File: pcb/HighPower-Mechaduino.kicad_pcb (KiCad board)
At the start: 2 copper layers, 60 x 60 mm, 132 parts, among them J1 SUPPLY, J2 STEPPER, P1 SWD, P2 USB, P3 PoStep25-32, P4 CONN_01X04, Q1 SSM3J328R, Q10 IPD079N06L3G, Q11 BSS138, Q2 BSS138, Q3 IPD079N06L3G, Q4 IPD079N06L3G, Q5 IPD079N06L3G, Q6 IPD079N06L3G, Q7 IPD079N06L3G, Q8 IPD079N06L3G, Q9 IPD079N06L3G, SW1 B3U-1000P, U1 AS5047D, U2 AP2112K-3.3TRG1, U3 AT24CS64-SSHM, U4 SAMD21G18A-A, U5 A4955GLPTR-T, U6 A4955GLPTR-T, U7 USBLC6-2SC6, U8 MCP16331T, U9 LM75BD, Y1 G83270022

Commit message: Update schematic
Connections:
- P1 pad 6: (no net) -> Net-(P1-Pad6)
- P1 pad 8: (no net) -> Net-(P1-Pad8)
- P2 pad 4: (no net) -> /Protected_USB_Supply/ID
- U1 pad 10: (no net) -> Net-(U1-Pad10)
- U1 pad 14: (no net) -> Net-(U1-Pad14)
- U1 pad 6: (no net) -> Net-(U1-Pad6)
- U1 pad 7: (no net) -> Net-(U1-Pad7)
- U1 pad 8: (no net) -> Net-(U1-Pad8)
- U1 pad 9: (no net) -> Net-(U1-Pad9)
- U4 pad 14: (no net) -> /Arduino_Zero_Base/Arduino_D3
- U4 pad 15: (no net) -> /Arduino_Zero_Base/Arduino_D1
- U4 pad 16: (no net) -> /Arduino_Zero_Base/Arduino_D0
- U4 pad 22: (no net) -> Net-(U4-Pad22)
- U4 pad 39: (no net) -> /Arduino_Zero_Base/Arduino_TX_LED
- U4 pad 41: (no net) -> /Arduino_Zero_Base/Arduino_USB_HOST_ENABLED
- U4 pad 48: (no net) -> /Arduino_Zero_Base/Arduino_RX_LED
- U5 pad 9: (no net) -> /PWM_Bridge_A4955-A/SLEEPn
- U6 pad 9: (no net) -> /PWM_Bridge_A4955-B/SLEEPn
- U9 pad 3: (no net) -> Net-(U9-Pad3)
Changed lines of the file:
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@@
   (general
     (links 293)
-    (no_connects 1)
+    (no_connects 0)
     (area 119.924999 69.924999 180.075001 130.075001)
     (thickness 1.6)
@@
     (zones 0)
     (modules 132)
-    (nets 80)
+    (nets 99)
   )
   (page A4)
@@
   (net 78 /MCP16331_5V/Vfb)
   (net 79 "Net-(C33-Pad1)")
+  (net 80 "Net-(P1-Pad6)")
+  (net 81 "Net-(P1-Pad8)")
+  (net 82 "Net-(U1-Pad6)")
+  (net 83 "Net-(U1-Pad7)")
+  (net 84 "Net-(U1-Pad8)")
+  (net 85 "Net-(U1-Pad9)")
+  (net 86 "Net-(U1-Pad10)")
+  (net 87 "Net-(U1-Pad14)")
+  (net 88 /PWM_Bridge_A4955-A/SLEEPn)
+  (net 89 /PWM_Bridge_A4955-B/SLEEPn)
+  (net 90 "Net-(U9-Pad3)")
+  (net 91 /Arduino_Zero_Base/Arduino_D3)
+  (net 92 /Arduino_Zero_Base/Arduino_D1)
+  (net 93 /Arduino_Zero_Base/Arduino_D0)
+  (net 94 "Net-(U4-Pad22)")
+  (net 95 /Arduino_Zero_Base/Arduino_TX_LED)
+  (net 96 /Arduino_Zero_Base/Arduino_USB_HOST_ENABLED)
+  (net 97 /Arduino_Zero_Base/Arduino_RX_LED)
+  (net 98 /Protected_USB_Supply/ID)
   (net_class Default "Dies ist die voreingestellte Netzklasse."
     (clearance 0.15)
@@
     (add_net /A_IN)
     (add_net /Arduino_Zero_Base/Arduino_AREF)
+    (add_net /Arduino_Zero_Base/Arduino_D0)
+    (add_net /Arduino_Zero_Base/Arduino_D1)
+    (add_net /Arduino_Zero_Base/Arduino_D3)
     (add_net /Arduino_Zero_Base/Arduino_RXD)
+    (add_net /Arduino_Zero_Base/Arduino_RX_LED)
     (add_net /Arduino_Zero_Base/Arduino_TXD)
+    (add_net /Arduino_Zero_Base/Arduino_TX_LED)
+    (add_net /Arduino_Zero_Base/Arduino_USB_HOST_ENABLED)
     (add_net /IN1)
     (add_net /IN2)
@@
     (add_net /OCLn1)
     (add_net /OCLn2)
+    (add_net /PWM_Bridge_A4955-A/SLEEPn)
     (add_net /PWM_Bridge_A4955-A/VREF)
+    (add_net /PWM_Bridge_A4955-B/SLEEPn)
     (add_net /PWM_Bridge_A4955-B/VREF)
+    (add_net /Protected_USB_Supply/ID)
     (add_net /Protected_USB_Supply/VBUS)
     (add_net /RESET)
@@
     (add_net "Net-(F2-Pad1)")
     (add_net "Net-(L2-Pad1)")
+    (add_net "Net-(P1-Pad6)")
+    (add_net "Net-(P1-Pad8)")
     (add_net "Net-(P3-Pad7)")
     (add_net "Net-(Q1-Pad1)")
@@
     (add_net "Net-(R18-Pad1)")
     (add_net "Net-(R4-Pad1)")
+    (add_net "Net-(U1-Pad10)")
+    (add_net "Net-(U1-Pad14)")
+    (add_net "Net-(U1-Pad6)")
+    (add_net "Net-(U1-Pad7)")
+    (add_net "Net-(U1-Pad8)")
+    (add_net "Net-(U1-Pad9)")
+    (add_net "Net-(U4-Pad22)")
+    (add_net "Net-(U9-Pad3)")
     (add_net VDD)
   )
@@
     (pad 4 smd rect (at -2.7 1.905 180) (size 1.55 0.6) (layers F.Cu F.Paste F.Mask)
       (net 1 GND))
-    (pad 3 smd rect (at -2.7 0.635 180) (size 1.55 0.6) (layers F.Cu F.Paste F.Mask))
+    (pad 3 smd rect (at -2.7 0.635 180) (size 1.55 0.6) (layers F.Cu F.Paste F.Mask)
+      (net 90 "Net-(U9-Pad3)"))
     (pad 2 smd rect (at -2.7 -0.635 180) (size 1.55 0.6) (layers F.Cu F.Paste F.Mask)
       (net 52 /SCL))
@@
     (pad 4 thru_hole circle (at 1.27 1.27 270) (size 1.05 1.05) (drill 0.65) (layers *.Cu *.Mask F.SilkS)
       (net 28 /SWCLK))
-    (pad 6 thru_hole circle (at 1.27 2.54 270) (size 1.05 1.05) (drill 0.65) (layers *.Cu *.Mask F.SilkS))
-    (pad 8 thru_hole circle (at 1.27 3.81 270) (size 1.05 1.05) (drill 0.65) (layers *.Cu *.Mask F.SilkS))
+    (pad 6 thru_hole circle (at 1.27 2.54 270) (size 1.05 1.05) (drill 0.65) (layers *.Cu *.Mask F.SilkS)
+      (net 80 "Net-(P1-Pad6)"))
+    (pad 8 thru_hole circle (at 1.27 3.81 270) (size 1.05 1.05) (drill 0.65) (layers *.Cu *.Mask F.SilkS)
+      (net 81 "Net-(P1-Pad8)"))
     (pad 10 thru_hole circle (at 1.27 5.08 270) (size 1.05 1.05) (drill 0.65) (layers *.Cu *.Mask F.SilkS)
       (net 29 /RESET))
@@
     (pad 3 smd rect (at -0.0009 -1.5 270) (size 1.65 0.4) (layers F.Cu F.Paste F.Mask)
       (net 32 /USB_D+))
-    (pad 4 smd rect (at 0.65 -1.5 270) (size 1.65 0.4) (layers F.Cu F.Paste F.Mask))
+    (pad 4 smd rect (at 0.65 -1.5 270) (size 1.65 0.4) (layers F.Cu F.Paste F.Mask)
+      (net 98 /Protected_USB_Supply/ID))
     (pad 5 smd rect (at 1.3 -1.5 270) (size 1.65 0.4) (layers F.Cu F.Paste F.Mask)
       (net 1 GND))
@@
     (pad 5 smd rect (at -2.95 -0.65 180) (size 1.45 0.45) (layers B.Cu B.Paste B.Mask)
       (net 1 GND))
-    (pad 6 smd rect (at -2.95 -1.3 180) (size 1.45 0.45) (layers B.Cu B.Paste B.Mask))
-    (pad 7 smd rect (at -2.95 -1.95 180) (size 1.45 0.45) (layers B.Cu B.Paste B.Mask))
-    (pad 8 smd rect (at 2.95 -1.95 180) (size 1.45 0.45) (layers B.Cu B.Paste B.Mask))
-    (pad 9 smd rect (at 2.95 -1.3 180) (size 1.45 0.45) (layers B.Cu B.Paste B.Mask))
-    (pad 10 smd rect (at 2.95 -0.65 180) (size 1.45 0.45) (layers B.Cu B.Paste B.Mask))
+    (pad 6 smd rect (at -2.95 -1.3 180) (size 1.45 0.45) (layers B.Cu B.Paste B.Mask)
+      (net 82 "Net-(U1-Pad6)"))
+    (pad 7 smd rect (at -2.95 -1.95 180) (size 1.45 0.45) (layers B.Cu B.Paste B.Mask)
+      (net 83 "Net-(U1-Pad7)"))
+    (pad 8 smd rect (at 2.95 -1.95 180) (size 1.45 0.45) (layers B.Cu B.Paste B.Mask)
+      (net 84 "Net-(U1-Pad8)"))
+    (pad 9 smd rect (at 2.95 -1.3 180) (size 1.45 0.45) (layers B.Cu B.Paste B.Mask)
+      (net 85 "Net-(U1-Pad9)"))
+    (pad 10 smd rect (at 2.95 -0.65 180) (size 1.45 0.45) (layers B.Cu B.Paste B.Mask)
+      (net 86 "Net-(U1-Pad10)"))
     (pad 11 smd rect (at 2.95 0 180) (size 1.45 0.45) (layers B.Cu B.Paste B.Mask)
       (net 3 +3V3))
@@
     (pad 13 smd rect (at 2.95 1.3 180) (size 1.45 0.45) (layers B.Cu B.Paste B.Mask)
       (net 1 GND))
-    (pad 14 smd rect (at 2.95 1.95 180) (size 1.45 0.45) (layers B.Cu B.Paste B.Mask))
+    (pad 14 smd rect (at 2.95 1.95 180) (size 1.45 0.45) (layers B.Cu B.Paste B.Mask)
+      (net 87 "Net-(U1-Pad14)"))
     (model Housings_SSOP.3dshapes/TSSOP-14_4.4x5mm_Pitch0.65mm.wrl
       (at (xyz 0 0 0))
@@
     (pad 13 smd rect (at -2.75 4.35 135) (size 1.3 0.25) (layers F.Cu F.Paste F.Mask)
       (net 49 /VREF2))
-    (pad 14 smd rect (at -2.25 4.35 135) (size 1.3 0.25) (layers F.Cu F.Paste F.Mask))
-    (pad 15 smd rect (at -1.749999 4.35 135) (size 1.3 0.25) (layers F.Cu F.Paste F.Mask))
-    (pad 16 smd rect (at -1.25 4.35 135) (size 1.3 0.25) (layers F.Cu F.Paste F.Mask))
+    (pad 14 smd rect (at -2.25 4.35 135) (size 1.3 0.25) (layers F.Cu F.Paste F.Mask)
+      (net 91 /Arduino_Zero_Base/Arduino_D3))
+    (pad 15 smd rect (at -1.749999 4.35 135) (size 1.3 0.25) (layers F.Cu F.Paste F.Mask)
+      (net 92 /Arduino_Zero_Base/Arduino_D1))
+    (pad 16 smd rect (at -1.25 4.35 135) (size 1.3 0.25) (layers F.Cu F.Paste F.Mask)
+      (net 93 /Arduino_Zero_Base/Arduino_D0))
     (pad 17 smd rect (at -0.750001 4.35 135) (size 1.3 0.25) (layers F.Cu F.Paste F.Mask)
       (net 3 +3V3))
@@
     (pad 21 smd rect (at 1.25 4.35 135) (size 1.3 0.25) (layers F.Cu F.Paste F.Mask)
       (net 57 /SPI_MISO))
-    (pad 22 smd rect (at 1.749999 4.35 135) (size 1.3 0.25) (layers F.Cu F.Paste F.Mask))
+    (pad 22 smd rect (at 1.749999 4.35 135) (size 1.3 0.25) (layers F.Cu F.Paste F.Mask)
+      (net 94 "Net-(U4-Pad22)"))
     (pad 23 smd rect (at 2.25 4.35 135) (size 1.3 0.25) (layers F.Cu F.Paste F.Mask)
       (net 46 /STP_ERROR))
@@
     (pad 38 smd rect (at 2.25 -4.35 135) (size 1.3 0.25) (layers F.Cu F.Paste F.Mask)
       (net 64 /Arduino_Zero_Base/Arduino_RXD))
-    (pad 39 smd rect (at 1.749999 -4.35 135) (size 1.3 0.25) (layers F.Cu F.Paste F.Mask))
+    (pad 39 smd rect (at 1.749999 -4.35 135) (size 1.3 0.25) (layers F.Cu F.Paste F.Mask)
+      (net 95 /Arduino_Zero_Base/Arduino_TX_LED))
     (pad 40 smd rect (at 1.25 -4.35 135) (size 1.3 0.25) (layers F.Cu F.Paste F.Mask)
       (net 50 "Net-(R11-Pad2)"))
-    (pad 41 smd rect (at 0.750001 -4.35 135) (size 1.3 0.25) (layers F.Cu F.Paste F.Mask))
+    (pad 41 smd rect (at 0.750001 -4.35 135) (size 1.3 0.25) (layers F.Cu F.Paste F.Mask)
+      (net 96 /Arduino_Zero_Base/Arduino_USB_HOST_ENABLED))
     (pad 42 smd rect (at 0.25 -4.35 135) (size 1.3 0.25) (layers F.Cu F.Paste F.Mask)
       (net 1 GND))
@@
     (pad 47 smd rect (at -2.25 -4.35 135) (size 1.3 0.25) (layers F.Cu F.Paste F.Mask)
       (net 77 /A_IN))
-    (pad 48 smd rect (at -2.75 -4.35 135) (size 1.3 0.25) (layers F.Cu F.Paste F.Mask))
+    (pad 48 smd rect (at -2.75 -4.35 135) (size 1.3 0.25) (layers F.Cu F.Paste F.Mask)
+      (net 97 /Arduino_Zero_Base/Arduino_RX_LED))
     (model Housings_QFP.3dshapes/TQFP-48_7x7mm_Pitch0.5mm.wrl
       (at (xyz 0 0 0))
@@
     (pad 10 smd rect (at -2.95 -2.925) (size 1.45 0.45) (layers B.Cu B.Paste B.Mask)
       (net 37 "Net-(Q4-Pad3)"))
-    (pad 9 smd rect (at -2.95 -2.275) (size 1.45 0.45) (layers B.Cu B.Paste B.Mask))
+    (pad 9 smd rect (at -2.95 -2.275) (size 1.45 0.45) (layers B.Cu B.Paste B.Mask)
+      (net 88 /PWM_Bridge_A4955-A/SLEEPn))
     (pad 8 smd rect (at -2.95 -1.625) (size 1.45 0.45) (layers B.Cu B.Paste B.Mask)
       (net 53 "Net-(R15-Pad1)"))
@@
     (pad 8 smd rect (at -2.95 -1.625 270) (size 1.45 0.45) (layers B.Cu B.Paste B.Mask)
       (net 54 "Net-(R18-Pad1)"))
-    (pad 9 smd rect (at -2.95 -2.275 270) (size 1.45 0.45) (layers B.Cu B.Paste B.Mask))
+    (pad 9 smd rect (at -2.95 -2.275 270) (size 1.45 0.45) (layers B.Cu B.Paste B.Mask)
+      (net 89 /PWM_Bridge_A4955-B/SLEEPn))
     (pad 10 smd rect (at -2.95 -2.925 270) (size 1.45 0.45) (layers B.Cu B.Paste B.Mask)
       (net 42 "Net-(Q10-Pad3)"))

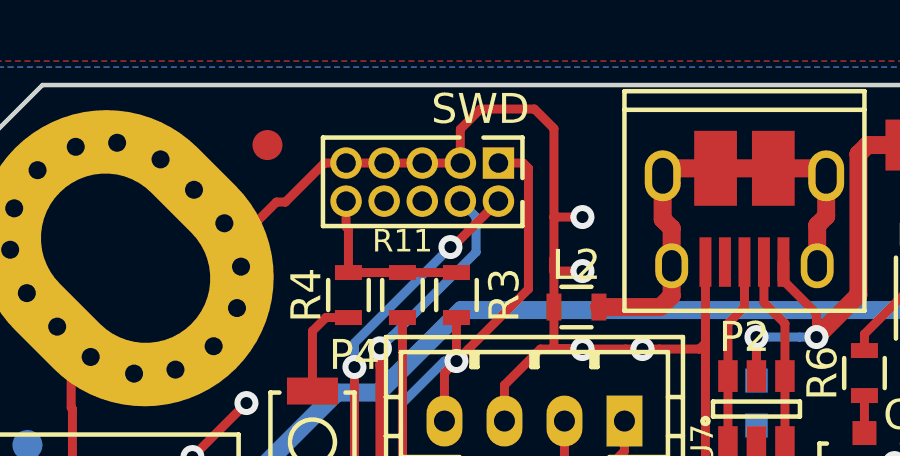
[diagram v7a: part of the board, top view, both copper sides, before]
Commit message: Fix #13
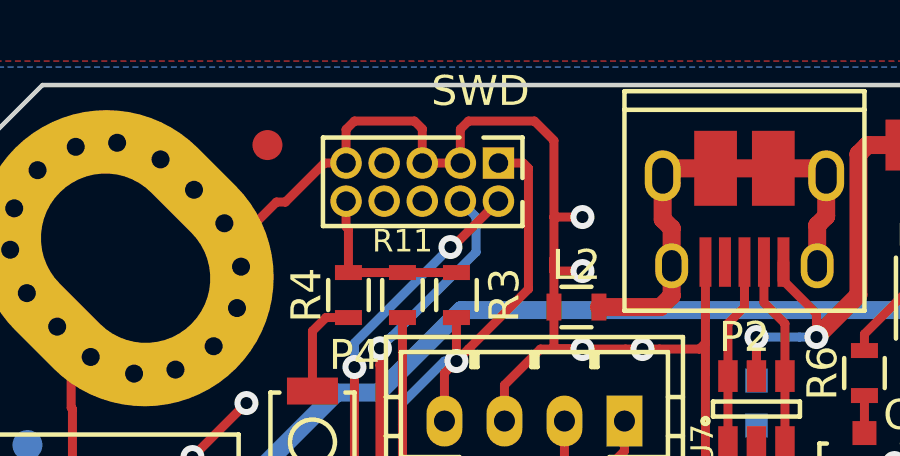
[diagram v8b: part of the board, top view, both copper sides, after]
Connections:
- P1 pad 6: Net-(P1-Pad6) -> (no net)
- P1 pad 7: GND -> (no net)
- P1 pad 8: Net-(P1-Pad8) -> (no net)
- P2 pad 4: /Protected_USB_Supply/ID -> (no net)
- U1 pad 10: Net-(U1-Pad10) -> (no net)
- U1 pad 14: Net-(U1-Pad14) -> (no net)
- U1 pad 6: Net-(U1-Pad6) -> (no net)
- U1 pad 7: Net-(U1-Pad7) -> (no net)
- U1 pad 8: Net-(U1-Pad8) -> (no net)
- U1 pad 9: Net-(U1-Pad9) -> (no net)
- U4 pad 14: /Arduino_Zero_Base/Arduino_D3 -> (no net)
- U4 pad 15: /Arduino_Zero_Base/Arduino_D1 -> (no net)
- U4 pad 16: /Arduino_Zero_Base/Arduino_D0 -> (no net)
- U4 pad 22: Net-(U4-Pad22) -> (no net)
- U4 pad 39: /Arduino_Zero_Base/Arduino_TX_LED -> (no net)
- U4 pad 41: /Arduino_Zero_Base/Arduino_USB_HOST_ENABLED -> (no net)
- U4 pad 48: /Arduino_Zero_Base/Arduino_RX_LED -> (no net)
- U5 pad 9: /PWM_Bridge_A4955-A/SLEEPn -> (no net)
- U6 pad 9: /PWM_Bridge_A4955-B/SLEEPn -> (no net)
- U9 pad 3: Net-(U9-Pad3) -> (no net)
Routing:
- net GND: track 540.3 -> 542.2 mm
